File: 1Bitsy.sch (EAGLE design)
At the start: 17 parts, among them IC1 74HC02D, IC4 74HC161, IC5 74HC161

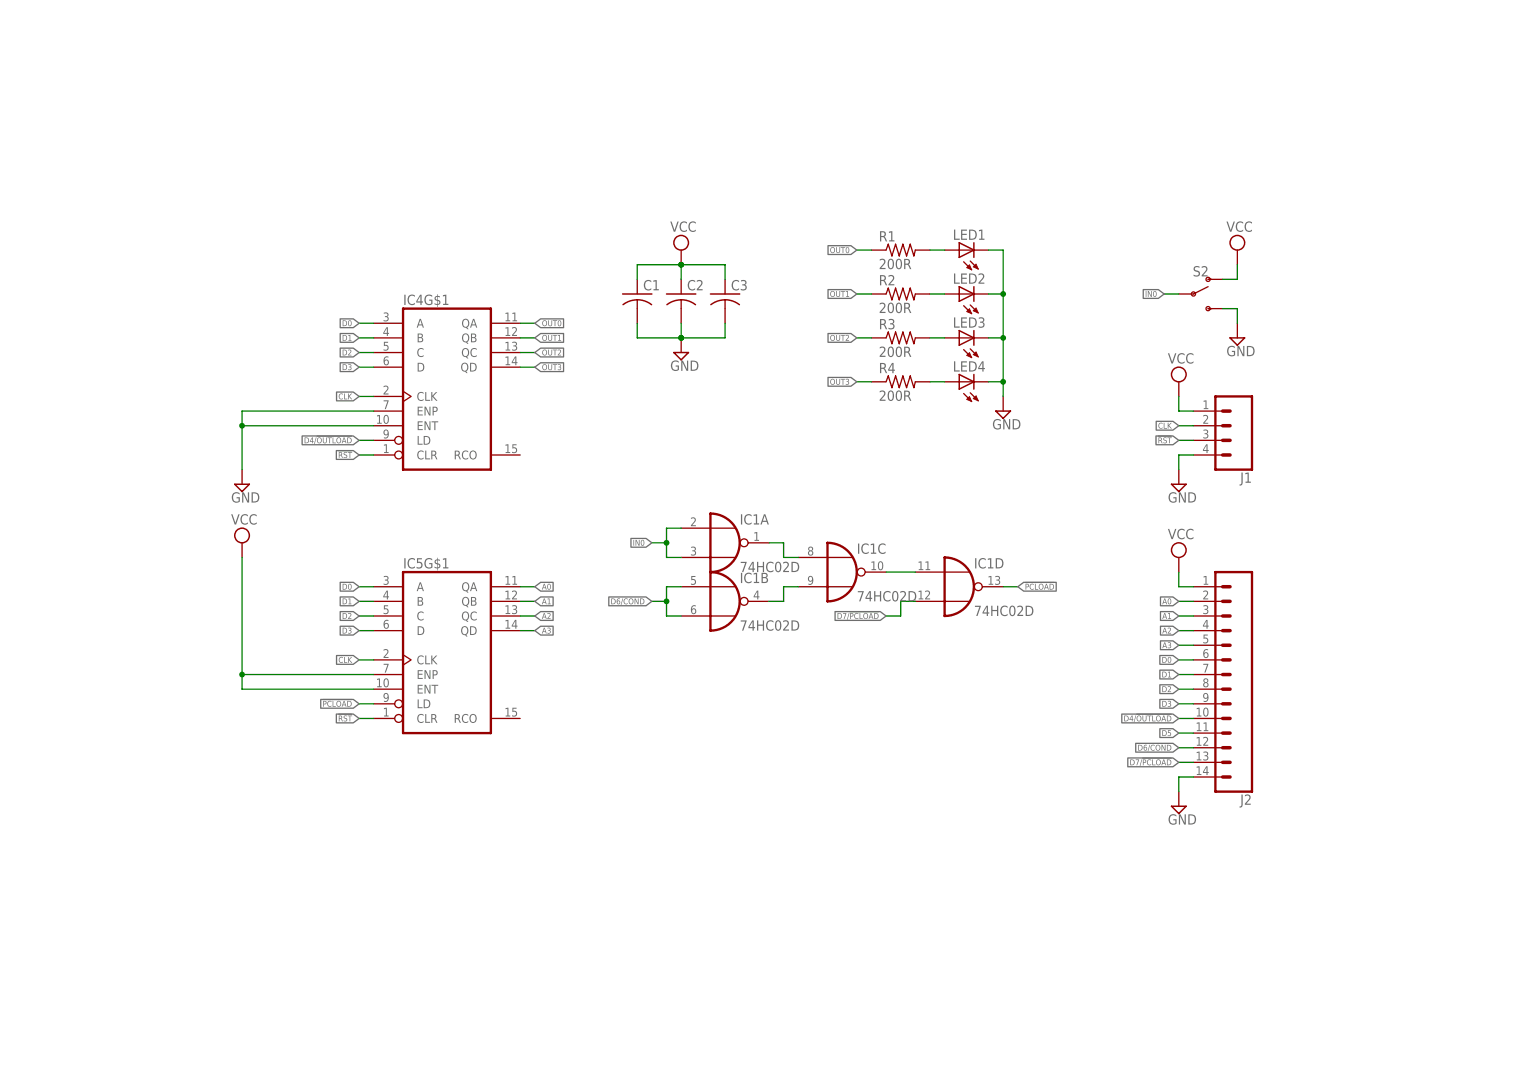
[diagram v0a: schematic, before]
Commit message: updated schematic to document purpose of each section
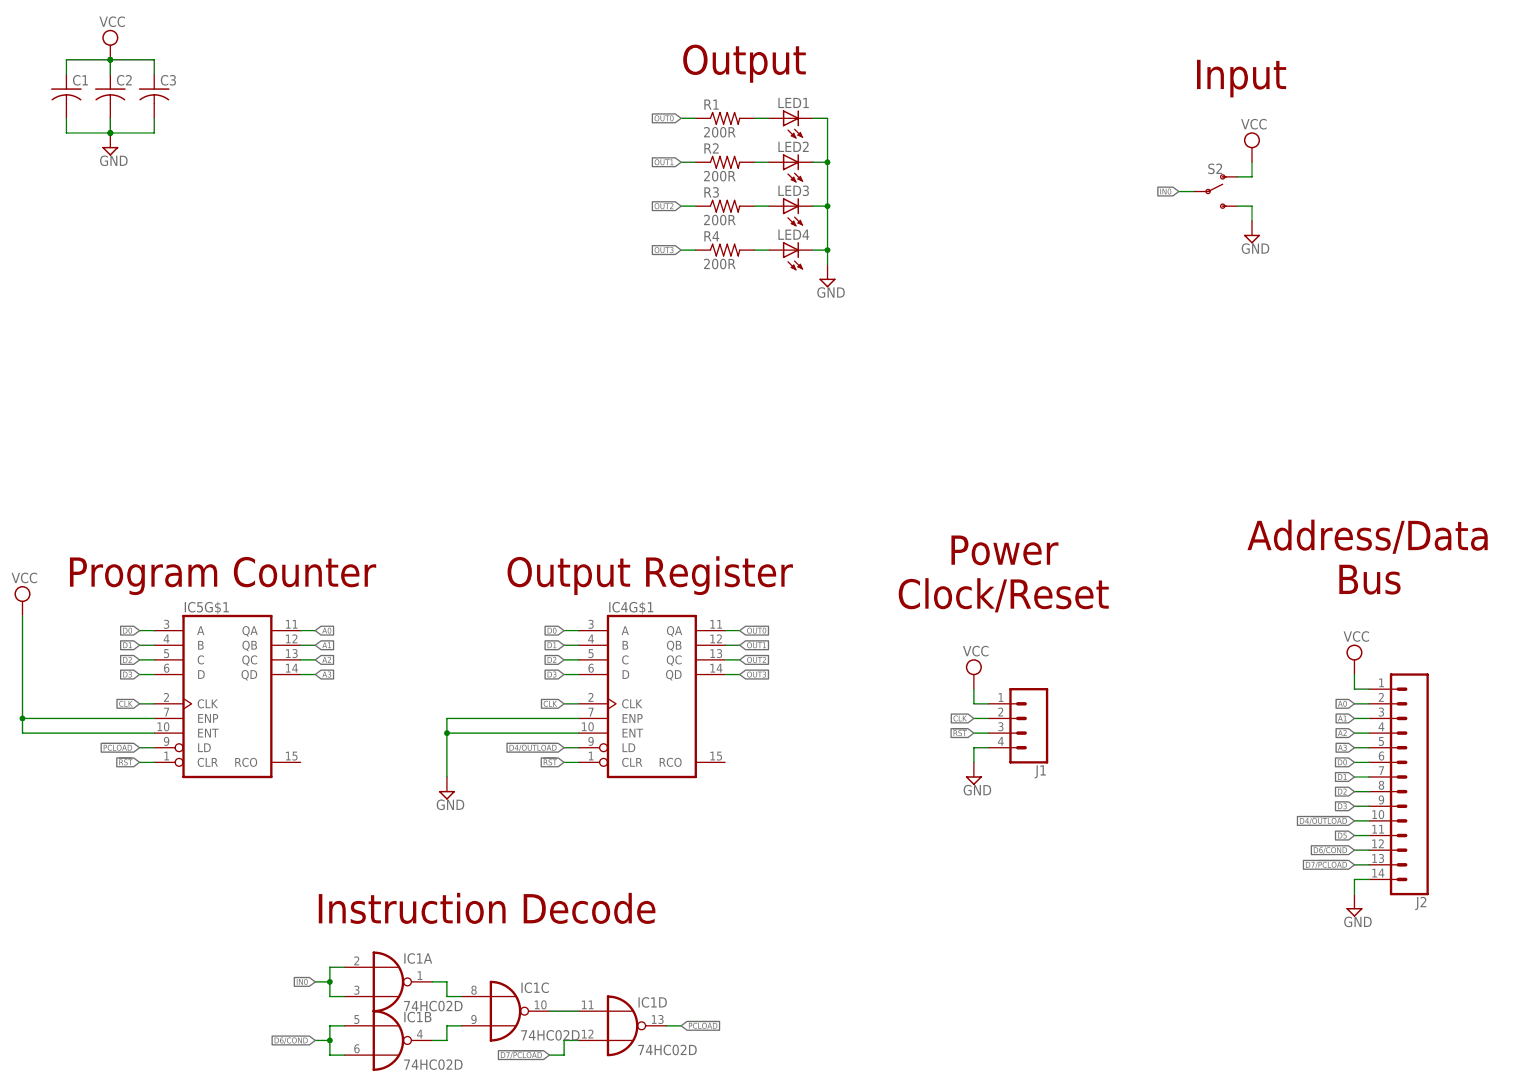
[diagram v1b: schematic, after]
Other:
- note added: "Address/Data Bus"
- note added: "Input"
- note added: "Instruction Decode"
- note added: "Output"
- note added: "Output Register"
- note added: "Power Clock/Reset"
- note added: "Program Counter"
- moved on the sheet: C1, C2, C3, IC1A, IC1B, IC1C, IC1D, IC4G$1, IC5G$1, J1, J2, LED1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
